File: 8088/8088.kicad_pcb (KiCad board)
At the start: 2 copper layers, 154.9 x 91.4 mm, 106 parts, among them CON1 BARREL_JACK, U1 8284, U10 2114, U11 ULN2803ADWR, U12 74LS14, U13 ULN2803ADWR, U14 ULN2803ADWR, U15 ULN2803ADWR, U16 7805, U2 8088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

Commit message: Added PCB images
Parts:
- added GND: GND, Pin_Headers:Pin_Header_Straight_2x02_Pitch2.54mm, F.Cu at (223.0, 49.5)
- added GND: GND, Pin_Headers:Pin_Header_Straight_2x02_Pitch2.54mm, F.Cu at (216.7, 49.5)
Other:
- outline, holes or cut-outs redrawn
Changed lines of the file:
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@@
     (area 62.23 19.05 255.270001 151.765001)
     (thickness 1.6)
-    (drawings 6)
+    (drawings 7)
     (tracks 1852)
     (zones 0)
-    (modules 106)
+    (modules 108)
     (nets 189)
   )
@@
     (visible_elements 7FFFFFFF)
     (pcbplotparams
-      (layerselection 0x00030_80000001)
+      (layerselection 0x01030_80000001)
       (usegerberextensions false)
       (excludeedgelayer true)
@@
       (padsonsilk false)
       (subtractmaskfromsilk false)
-      (outputformat 1)
+      (outputformat 4)
       (mirror false)
-      (drillshape 1)
+      (drillshape 0)
       (scaleselection 1)
-      (outputdirectory ""))
+      (outputdirectory documents/))
   )
   (net 0 "")
@@
     (add_net GND)
   )
+  (module Pin_Headers:Pin_Header_Straight_2x02_Pitch2.54mm (layer F.Cu)
+    (at 223.012 49.53)
+    (descr "Through hole straight pin header, 2x02, 2.54mm pitch, double rows")
+    (tags "Through hole pin header THT 2x02 2.54mm double row")
+    (fp_text reference GND (at 1.27 -2.33) (layer F.SilkS)
+      (effects (font (size 1 1) (thickness 0.15)))
+    )
+    (fp_text value GND (at 1.27 4.87) (layer F.Fab)
+      (effects (font (size 1 1) (thickness 0.15)))
+    )
+    (fp_line (start 0 -1.27) (end 3.81 -1.27) (layer F.Fab) (width 0.1))
+    (fp_line (start 3.81 -1.27) (end 3.81 3.81) (layer F.Fab) (width 0.1))
+    (fp_line (start 3.81 3.81) (end -1.27 3.81) (layer F.Fab) (width 0.1))
+    (fp_line (start -1.27 3.81) (end -1.27 0) (layer F.Fab) (width 0.1))
+    (fp_line (start -1.27 0) (end 0 -1.27) (layer F.Fab) (width 0.1))
+    (fp_line (start -1.33 3.87) (end 3.87 3.87) (layer F.SilkS) (width 0.12))
+    (fp_line (start -1.33 1.27) (end -1.33 3.87) (layer F.SilkS) (width 0.12))
+    (fp_line (start 3.87 -1.33) (end 3.87 3.87) (layer F.SilkS) (width 0.12))
+    (fp_line (start -1.33 1.27) (end 1.27 1.27) (layer F.SilkS) (width 0.12))
+    (fp_line (start 1.27 1.27) (end 1.27 -1.33) (layer F.SilkS) (width 0.12))
+    (fp_line (start 1.27 -1.33) (end 3.87 -1.33) (layer F.SilkS) (width 0.12))
+    (fp_line (start -1.33 0) (end -1.33 -1.33) (layer F.SilkS) (width 0.12))
+    (fp_line (start -1.33 -1.33) (end 0 -1.33) (layer F.SilkS) (width 0.12))
+    (fp_line (start -1.8 -1.8) (end -1.8 4.35) (layer F.CrtYd) (width 0.05))
+    (fp_line (start -1.8 4.35) (end 4.35 4.35) (layer F.CrtYd) (width 0.05))
+    (fp_line (start 4.35 4.35) (end 4.35 -1.8) (layer F.CrtYd) (width 0.05))
+    (fp_line (start 4.35 -1.8) (end -1.8 -1.8) (layer F.CrtYd) (width 0.05))
+    (fp_text user %R (at 1.27 1.27 90) (layer F.Fab)
+      (effects (font (size 1 1) (thickness 0.15)))
+    )
+    (pad 1 thru_hole rect (at 0 0) (size 1.7 1.7) (drill 1) (layers *.Cu *.Mask)
+      (net 2 GND))
+    (pad 2 thru_hole oval (at 2.54 0) (size 1.7 1.7) (drill 1) (layers *.Cu *.Mask)
+      (net 2 GND))
+    (pad 3 thru_hole oval (at 0 2.54) (size 1.7 1.7) (drill 1) (layers *.Cu *.Mask)
+      (net 2 GND))
+    (pad 4 thru_hole oval (at 2.54 2.54) (size 1.7 1.7) (drill 1) (layers *.Cu *.Mask)
+      (net 2 GND))
+    (model ${KISYS3DMOD}/Pin_Headers.3dshapes/Pin_Header_Straight_2x02_Pitch2.54mm.wrl
+      (at (xyz 0 0 0))
+      (scale (xyz 1 1 1))
+      (rotate (xyz 0 0 0))
+    )
+  )
+  (module Pin_Headers:Pin_Header_Straight_2x02_Pitch2.54mm (layer F.Cu)
+    (at 216.662 49.53)
+    (descr "Through hole straight pin header, 2x02, 2.54mm pitch, double rows")
+    (tags "Through hole pin header THT 2x02 2.54mm double row")
+    (fp_text reference GND (at 1.27 -2.33) (layer F.SilkS)
+      (effects (font (size 1 1) (thickness 0.15)))
+    )
+    (fp_text value GND (at 1.27 4.87) (layer F.Fab)
+      (effects (font (size 1 1) (thickness 0.15)))
+    )
+    (fp_line (start 0 -1.27) (end 3.81 -1.27) (layer F.Fab) (width 0.1))
+    (fp_line (start 3.81 -1.27) (end 3.81 3.81) (layer F.Fab) (width 0.1))
+    (fp_line (start 3.81 3.81) (end -1.27 3.81) (layer F.Fab) (width 0.1))
+    (fp_line (start -1.27 3.81) (end -1.27 0) (layer F.Fab) (width 0.1))
+    (fp_line (start -1.27 0) (end 0 -1.27) (layer F.Fab) (width 0.1))
+    (fp_line (start -1.33 3.87) (end 3.87 3.87) (layer F.SilkS) (width 0.12))
+    (fp_line (start -1.33 1.27) (end -1.33 3.87) (layer F.SilkS) (width 0.12))
+    (fp_line (start 3.87 -1.33) (end 3.87 3.87) (layer F.SilkS) (width 0.12))
+    (fp_line (start -1.33 1.27) (end 1.27 1.27) (layer F.SilkS) (width 0.12))
+    (fp_line (start 1.27 1.27) (end 1.27 -1.33) (layer F.SilkS) (width 0.12))
+    (fp_line (start 1.27 -1.33) (end 3.87 -1.33) (layer F.SilkS) (width 0.12))
+    (fp_line (start -1.33 0) (end -1.33 -1.33) (layer F.SilkS) (width 0.12))
+    (fp_line (start -1.33 -1.33) (end 0 -1.33) (layer F.SilkS) (width 0.12))
+    (fp_line (start -1.8 -1.8) (end -1.8 4.35) (layer F.CrtYd) (width 0.05))
+    (fp_line (start -1.8 4.35) (end 4.35 4.35) (layer F.CrtYd) (width 0.05))
+    (fp_line (start 4.35 4.35) (end 4.35 -1.8) (layer F.CrtYd) (width 0.05))
+    (fp_line (start 4.35 -1.8) (end -1.8 -1.8) (layer F.CrtYd) (width 0.05))
+    (fp_text user %R (at 1.27 1.27 90) (layer F.Fab)
+      (effects (font (size 1 1) (thickness 0.15)))
+    )
+    (pad 1 thru_hole rect (at 0 0) (size 1.7 1.7) (drill 1) (layers *.Cu *.Mask)
+      (net 2 GND))
+    (pad 2 thru_hole oval (at 2.54 0) (size 1.7 1.7) (drill 1) (layers *.Cu *.Mask)
+      (net 2 GND))
+    (pad 3 thru_hole oval (at 0 2.54) (size 1.7 1.7) (drill 1) (layers *.Cu *.Mask)
+      (net 2 GND))
+    (pad 4 thru_hole oval (at 2.54 2.54) (size 1.7 1.7) (drill 1) (layers *.Cu *.Mask)
+      (net 2 GND))
+    (model ${KISYS3DMOD}/Pin_Headers.3dshapes/Pin_Header_Straight_2x02_Pitch2.54mm.wrl
+      (at (xyz 0 0 0))
+      (scale (xyz 1 1 1))
+      (rotate (xyz 0 0 0))
+    )
+  )
   (module LEDs:LED_1206_HandSoldering (layer F.Cu)
     (at 185.274268 50.672284 270)
@@
     )
   )
-  (gr_line (start 76.2 132.715) (end 231.14 132.588) (layer Edge.Cuts) (width 0.15))
+  (dimension 91.44 (width 0.0762) (layer Eco2.User)
+    (gr_text "91.440 mm" (at 73.1012 86.868 270) (layer Eco2.User)
+      (effects (font (size 0.8128 0.8128) (thickness 0.0762)))
+    )
+    (feature1 (pts (xy 76.2 132.588) (xy 72.5424 132.588)))
+    (feature2 (pts (xy 76.2 41.148) (xy 72.5424 41.148)))
+    (crossbar (pts (xy 73.66 41.148) (xy 73.66 132.588)))
+    (arrow1a (pts (xy 73.66 132.588) (xy 73.073579 131.461496)))
+    (arrow1b (pts (xy 73.66 132.588) (xy 74.246421 131.461496)))
+    (arrow2a (pts (xy 73.66 41.148) (xy 73.073579 42.274504)))
+    (arrow2b (pts (xy 73.66 41.148) (xy 74.246421 42.274504)))
+  )
+  (gr_line (start 76.2 132.588) (end 231.14 132.588) (layer Edge.Cuts) (width 0.15))
   (dimension 154.94 (width 0.0762) (layer Eco2.User)
     (gr_text "154.940 mm" (at 153.67 31.8262) (layer Eco2.User)
@@
     (arrow2b (pts (xy 76.2 32.385) (xy 77.326504 31.798579)))
   )
-  (gr_line (start 76.2 132.715) (end 76.2 41.275) (layer Edge.Cuts) (width 0.15))
-  (gr_line (start 231.14 41.275) (end 231.14 132.715) (layer Edge.Cuts) (width 0.15))
-  (gr_line (start 220.98 41.275) (end 231.14 41.275) (layer Edge.Cuts) (width 0.15))
-  (gr_line (start 76.2 41.275) (end 220.98 41.275) (layer Edge.Cuts) (width 0.15))
+  (gr_line (start 76.2 132.588) (end 76.2 41.148) (layer Edge.Cuts) (width 0.15))
+  (gr_line (start 231.14 41.148) (end 231.14 132.588) (layer Edge.Cuts) (width 0.15))
+  (gr_line (start 220.98 41.148) (end 231.14 41.148) (layer Edge.Cuts) (width 0.15))
+  (gr_line (start 76.2 41.148) (end 220.98 41.148) (layer Edge.Cuts) (width 0.15))
   (segment (start 119.40806 48.641108) (end 119.323062 48.641108) (width 0.25) (layer B.Cu) (net 0))
   (segment (start 138.429892 48.641108) (end 138.394168 48.641108) (width 0.25) (layer B.Cu) (net 0))

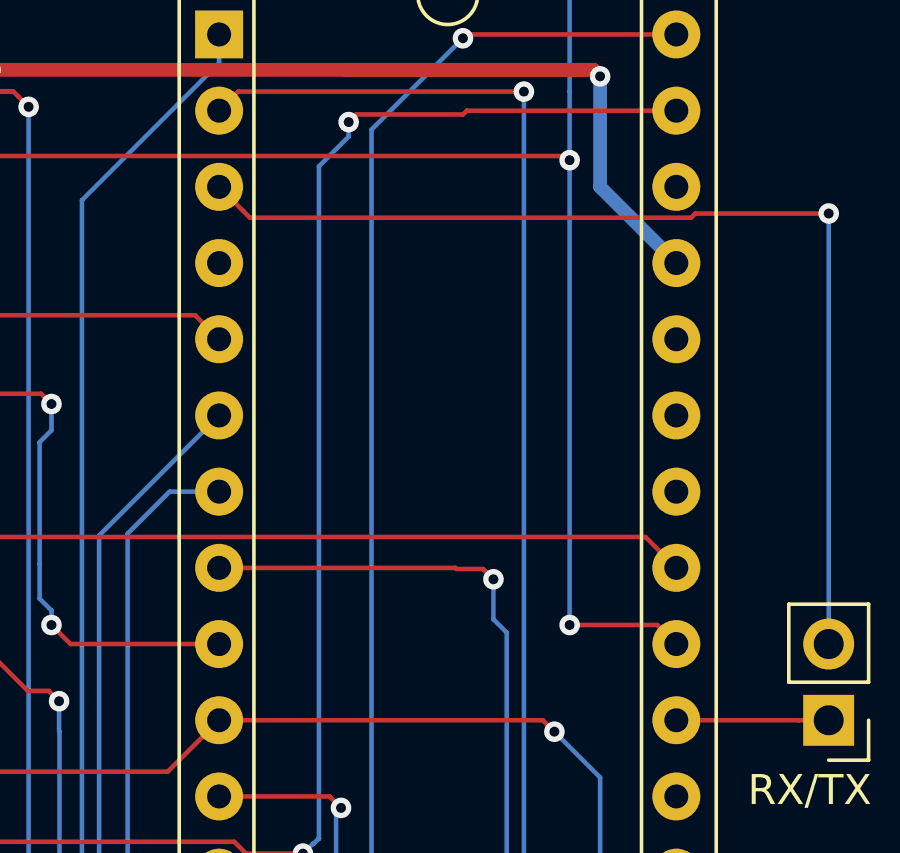
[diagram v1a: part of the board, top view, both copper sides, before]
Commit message: Fixed pin 26 discrepency on PCB layout
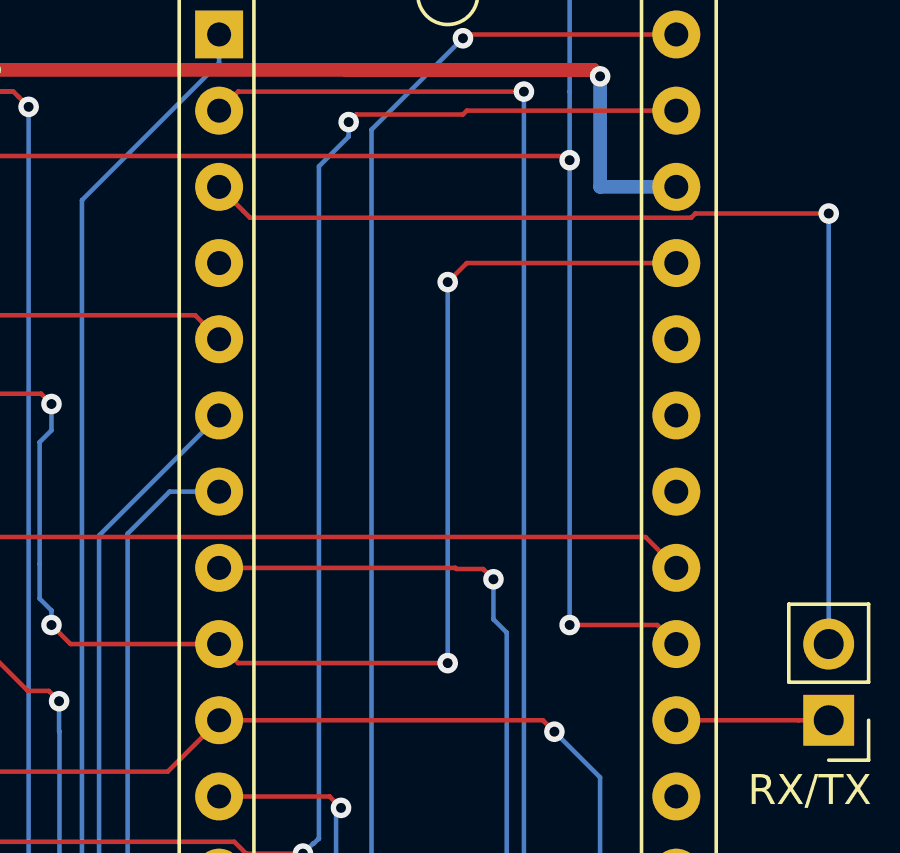
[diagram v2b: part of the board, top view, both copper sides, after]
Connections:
- U5 pad 25: +5V -> Net-(U4-Pad6)
- U5 pad 26: (no net) -> +5V
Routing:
- net Net-(U4-Pad6): track 41.3 -> 69.7 mm, vias 2 -> 4
- net +5V: track 426.3 -> 425.2 mm
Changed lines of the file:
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@@
-(kicad_pcb (version 4) (host pcbnew 4.0.3-stable)
+(kicad_pcb (version 4) (host pcbnew 4.0.6)
   (general
-    (links 344)
+    (links 352)
     (no_connects 0)
     (area 62.23 19.05 255.270001 151.765001)
     (thickness 1.6)
     (drawings 7)
-    (tracks 1852)
+    (tracks 1859)
     (zones 0)
     (modules 108)
@@
     (mod_text_size 0.8128 0.8128)
     (mod_text_width 0.0762)
-    (pad_size 1.2 2.2)
-    (pad_drill 0.9)
+    (pad_size 1.6 1.6)
+    (pad_drill 0.8)
     (pad_to_mask_clearance 0)
     (aux_axis_origin 0 0)
@@
       (net 167 "Net-(U5-Pad11)"))
     (pad 25 thru_hole oval (at 15.24 7.62) (size 1.6 1.6) (drill 0.8) (layers *.Cu *.Mask)
-      (net 7 +5V))
+      (net 160 "Net-(U4-Pad6)"))
     (pad 12 thru_hole oval (at 0 27.94) (size 1.6 1.6) (drill 0.8) (layers *.Cu *.Mask)
       (net 168 /A0))
-    (pad 26 thru_hole oval (at 15.24 5.08) (size 1.6 1.6) (drill 0.8) (layers *.Cu *.Mask))
+    (pad 26 thru_hole oval (at 15.24 5.08) (size 1.6 1.6) (drill 0.8) (layers *.Cu *.Mask)
+      (net 7 +5V))
     (pad 13 thru_hole oval (at 0 30.48) (size 1.6 1.6) (drill 0.8) (layers *.Cu *.Mask)
       (net 148 /~RD))
@@
   (segment (start 102.235 126.12) (end 100.33 124.215) (width 0.4572) (layer B.Cu) (net 6))
   (segment (start 102.235 129.92) (end 102.235 126.62) (width 0.4572) (layer F.Cu) (net 6))
+  (segment (start 220.98 69.215) (end 223.52 69.215) (width 0.4572) (layer B.Cu) (net 7))
   (segment (start 95.25 92.71) (end 95.25 93.9172) (width 0.4572) (layer F.Cu) (net 7))
   (segment (start 95.25 93.9172) (end 95.25 100.9318) (width 0.4572) (layer F.Cu) (net 7))
@@
   (via (at 141.732 72.644) (size 0.6858) (drill 0.3302) (layers F.Cu B.Cu) (net 7))
   (segment (start 220.98 65.532) (end 220.98 69.215) (width 0.4572) (layer B.Cu) (net 7))
-  (segment (start 220.98 69.215) (end 223.52 71.755) (width 0.4572) (layer B.Cu) (net 7))
   (segment (start 212.509001 65.316001) (end 220.764001 65.316001) (width 0.4572) (layer F.Cu) (net 7))
   (via (at 220.98 65.532) (size 0.6858) (drill 0.3302) (layers F.Cu B.Cu) (net 7))
@@
   (segment (start 153.035 66.675) (end 153.416 67.056) (width 0.1524) (layer F.Cu) (net 159))
   (via (at 154.94 67.056) (size 0.6858) (drill 0.3302) (layers F.Cu B.Cu) (net 159))
+  (segment (start 215.9 85.09) (end 208.915 85.09) (width 0.1524) (layer F.Cu) (net 160))
+  (segment (start 208.915 85.09) (end 208.28 84.455) (width 0.1524) (layer F.Cu) (net 160))
+  (segment (start 215.9 72.39) (end 215.9 85.09) (width 0.1524) (layer B.Cu) (net 160))
+  (via (at 215.9 85.09) (size 0.6858) (drill 0.3302) (layers F.Cu B.Cu) (net 160))
+  (segment (start 223.52 71.755) (end 216.535 71.755) (width 0.1524) (layer F.Cu) (net 160))
+  (segment (start 216.535 71.755) (end 215.9 72.39) (width 0.1524) (layer F.Cu) (net 160))
+  (via (at 215.9 72.39) (size 0.6858) (drill 0.3302) (layers F.Cu B.Cu) (net 160))
   (segment (start 193.590069 77.863601) (end 194.99967 76.454) (width 0.1524) (layer F.Cu) (net 160))
   (segment (start 194.99967 76.454) (end 195.062271 76.391399) (width 0.1524) (layer F.Cu) (net 160))
